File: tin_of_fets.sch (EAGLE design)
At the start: 49 parts, among them Q1 J112, Q2 J112, Q3 ZVN4306A, Q4 ZVN4306A, Q5 J112, Q6 J112, Q7 ZVN4306A, Q8 ZVN4306A, T1 ZTX694B

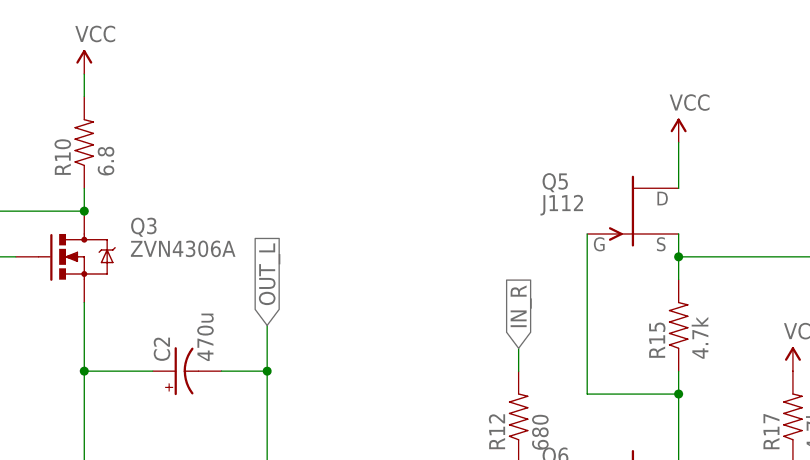
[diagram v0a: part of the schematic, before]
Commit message: Single bypass cap. No more room
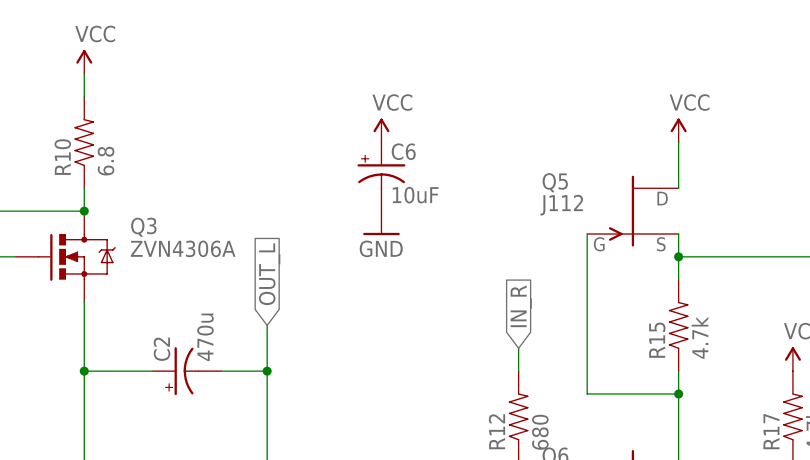
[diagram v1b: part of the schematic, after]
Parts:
- added C6: 10uF, SparkFun-Capacitors:CAP_POLPTH2
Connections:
- net GND: now also C6.-
- net VCC: now also C6.+
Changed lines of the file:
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@@
 <grid distance="0.1" unitdist="inch" unit="inch" style="lines" multiple="1" display="no" altdistance="0.01" altunitdist="inch" altunit="inch"/>
 <layers>
-<layer number="1" name="Top" color="4" fill="1" visible="yes" active="no"/>
-<layer number="16" name="Bottom" color="1" fill="1" visible="yes" active="no"/>
-<layer number="17" name="Pads" color="2" fill="1" visible="yes" active="no"/>
-<layer number="18" name="Vias" color="2" fill="1" visible="yes" active="no"/>
-<layer number="19" name="Unrouted" color="6" fill="1" visible="yes" active="no"/>
-<layer number="20" name="Dimension" color="15" fill="1" visible="yes" active="no"/>
-<layer number="21" name="tPlace" color="7" fill="1" visible="yes" active="no"/>
-<layer number="22" name="bPlace" color="7" fill="1" visible="yes" active="no"/>
-<layer number="23" name="tOrigins" color="15" fill="1" visible="yes" active="no"/>
-<layer number="24" name="bOrigins" color="15" fill="1" visible="yes" active="no"/>
-<layer number="25" name="tNames" color="7" fill="1" visible="yes" active="no"/>
-<layer number="26" name="bNames" color="7" fill="1" visible="yes" active="no"/>
-<layer number="27" name="tValues" color="7" fill="1" visible="yes" active="no"/>
-<layer number="28" name="bValues" color="7" fill="1" visible="yes" active="no"/>
+<layer number="1" name="Top" color="4" fill="1" visible="no" active="no"/>
+<layer number="16" name="Bottom" color="1" fill="1" visible="no" active="no"/>
+<layer number="17" name="Pads" color="2" fill="1" visible="no" active="no"/>
+<layer number="18" name="Vias" color="2" fill="1" visible="no" active="no"/>
+<layer number="19" name="Unrouted" color="6" fill="1" visible="no" active="no"/>
+<layer number="20" name="Dimension" color="15" fill="1" visible="no" active="no"/>
+<layer number="21" name="tPlace" color="7" fill="1" visible="no" active="no"/>
+<layer number="22" name="bPlace" color="7" fill="1" visible="no" active="no"/>
+<layer number="23" name="tOrigins" color="15" fill="1" visible="no" active="no"/>
+<layer number="24" name="bOrigins" color="15" fill="1" visible="no" active="no"/>
+<layer number="25" name="tNames" color="7" fill="1" visible="no" active="no"/>
+<layer number="26" name="bNames" color="7" fill="1" visible="no" active="no"/>
+<layer number="27" name="tValues" color="7" fill="1" visible="no" active="no"/>
+<layer number="28" name="bValues" color="7" fill="1" visible="no" active="no"/>
 <layer number="29" name="tStop" color="7" fill="3" visible="no" active="no"/>
 <layer number="30" name="bStop" color="7" fill="6" visible="no" active="no"/>
@@
 <layer number="35" name="tGlue" color="7" fill="4" visible="no" active="no"/>
 <layer number="36" name="bGlue" color="7" fill="5" visible="no" active="no"/>
-<layer number="37" name="tTest" color="7" fill="1" visible="yes" active="no"/>
-<layer number="38" name="bTest" color="7" fill="1" visible="yes" active="no"/>
+<layer number="37" name="tTest" color="7" fill="1" visible="no" active="no"/>
+<layer number="38" name="bTest" color="7" fill="1" visible="no" active="no"/>
 <layer number="39" name="tKeepout" color="4" fill="11" visible="no" active="no"/>
 <layer number="40" name="bKeepout" color="1" fill="11" visible="no" active="no"/>
@@
 <layer number="44" name="Drills" color="7" fill="1" visible="no" active="no"/>
 <layer number="45" name="Holes" color="7" fill="1" visible="no" active="no"/>
-<layer number="46" name="Milling" color="3" fill="1" visible="yes" active="no"/>
-<layer number="47" name="Measures" color="7" fill="1" visible="yes" active="no"/>
-<layer number="48" name="Document" color="7" fill="1" visible="yes" active="no"/>
-<layer number="49" name="Reference" color="7" fill="1" visible="yes" active="no"/>
-<layer number="50" name="dxf" color="7" fill="1" visible="yes" active="no"/>
-<layer number="51" name="tDocu" color="7" fill="1" visible="yes" active="no"/>
-<layer number="52" name="bDocu" color="7" fill="1" visible="yes" active="no"/>
-<layer number="53" name="tGND_GNDA" color="7" fill="9" visible="yes" active="no"/>
-<layer number="54" name="bGND_GNDA" color="1" fill="9" visible="yes" active="no"/>
-<layer number="56" name="wert" color="7" fill="1" visible="yes" active="no"/>
-<layer number="57" name="tCAD" color="7" fill="1" visible="yes" active="no"/>
-<layer number="59" name="tCarbon" color="7" fill="1" visible="yes" active="no"/>
-<layer number="60" name="bCarbon" color="7" fill="1" visible="yes" active="no"/>
+<layer number="46" name="Milling" color="3" fill="1" visible="no" active="no"/>
+<layer number="47" name="Measures" color="7" fill="1" visible="no" active="no"/>
+<layer number="48" name="Document" color="7" fill="1" visible="no" active="no"/>
+<layer number="49" name="Reference" color="7" fill="1" visible="no" active="no"/>
+<layer number="50" name="dxf" color="7" fill="1" visible="no" active="no"/>
+<layer number="51" name="tDocu" color="7" fill="1" visible="no" active="no"/>
+<layer number="52" name="bDocu" color="7" fill="1" visible="no" active="no"/>
+<layer number="53" name="tGND_GNDA" color="7" fill="9" visible="no" active="no"/>
+<layer number="54" name="bGND_GNDA" color="1" fill="9" visible="no" active="no"/>
+<layer number="56" name="wert" color="7" fill="1" visible="no" active="no"/>
+<layer number="57" name="tCAD" color="7" fill="1" visible="no" active="no"/>
+<layer number="59" name="tCarbon" color="7" fill="1" visible="no" active="no"/>
+<layer number="60" name="bCarbon" color="7" fill="1" visible="no" active="no"/>
 <layer number="90" name="Modules" color="5" fill="1" visible="yes" active="yes"/>
 <layer number="91" name="Nets" color="2" fill="1" visible="yes" active="yes"/>
@@
 <part name="J4" library="SparkFun-Connectors" deviceset="AUDIO-JACK" device="2.5MM"/>
 <part name="GND12" library="SparkFun-Aesthetics" deviceset="GND" device=""/>
+<part name="C6" library="SparkFun-Capacitors" deviceset="CAP_POL" device="PTH2" value="10uF"/>
+<part name="GND11" library="SparkFun-Aesthetics" deviceset="GND" device=""/>
+<part name="SUPPLY8" library="SparkFun-Aesthetics" deviceset="VCC" device=""/>
 </parts>
 <sheets>
@@
 <instance part="J4" gate="G$1" x="91.44" y="78.74"/>
 <instance part="GND12" gate="1" x="101.6" y="81.28" rot="R90"/>
+<instance part="C6" gate="G$1" x="139.7" y="162.56"/>
+<instance part="GND11" gate="1" x="139.7" y="154.94"/>
+<instance part="SUPPLY8" gate="G$1" x="139.7" y="165.1"/>
 </instances>
 <busses>
@@
 <junction x="96.52" y="81.28"/>
 </segment>
+<segment>
+<pinref part="C6" gate="G$1" pin="-"/>
+<pinref part="GND11" gate="1" pin="GND"/>
+</segment>
 </net>
 <net name="N$6" class="0">
@@
 <wire x1="210.82" y1="63.5" x2="218.44" y2="63.5" width="0.1524" layer="91"/>
 </segment>
-</net>
+<segment>
+<pinref part="C6" gate="G$1" pin="+"/>
+<pinref part="SUPPLY8" gate="G$1" pin="VCC"/>
+</segment>
+</net>

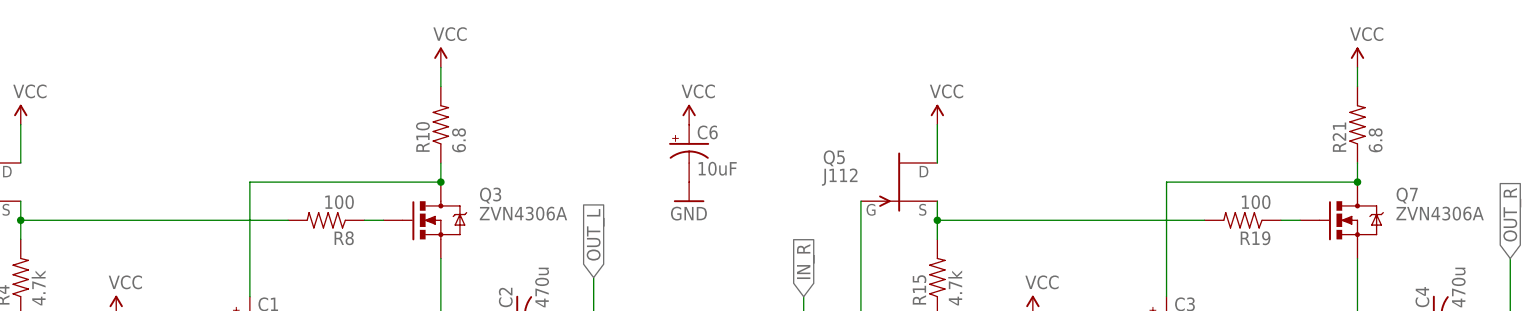
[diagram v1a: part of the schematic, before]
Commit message: Added pads for hand-wiring bypass caps
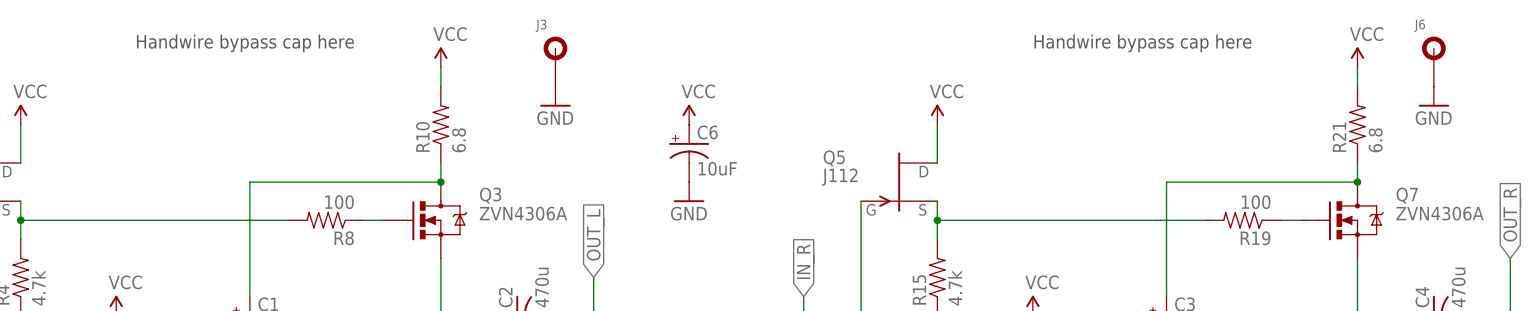
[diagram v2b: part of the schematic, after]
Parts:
- added J3, J6: PAD-NO-THERMAL, my:PAD-NO-THERMAL
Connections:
- net GND: now also J3.P$1, J6.P$1
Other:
- note added: "Handwire bypass cap here"
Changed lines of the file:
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@@
 <part name="GND11" library="SparkFun-Aesthetics" deviceset="GND" device=""/>
 <part name="SUPPLY8" library="SparkFun-Aesthetics" deviceset="VCC" device=""/>
+<part name="J3" library="my" deviceset="PAD-NO-THERMAL" device=""/>
+<part name="GND16" library="SparkFun-Aesthetics" deviceset="GND" device=""/>
+<part name="J6" library="my" deviceset="PAD-NO-THERMAL" device=""/>
+<part name="GND17" library="SparkFun-Aesthetics" deviceset="GND" device=""/>
 </parts>
 <sheets>
 <sheet>
 <plain>
+<text x="66.04" y="175.26" size="1.778" layer="97">Handwire bypass cap here</text>
+<text x="185.42" y="175.26" size="1.778" layer="97">Handwire bypass cap here</text>
 </plain>
 <instances>
@@
 <instance part="GND11" gate="1" x="139.7" y="154.94"/>
 <instance part="SUPPLY8" gate="G$1" x="139.7" y="165.1"/>
+<instance part="J3" gate="G$1" x="121.92" y="175.26"/>
+<instance part="GND16" gate="1" x="121.92" y="167.64"/>
+<instance part="J6" gate="G$1" x="238.76" y="175.26"/>
+<instance part="GND17" gate="1" x="238.76" y="167.64"/>
 </instances>
 <busses>
@@
 <pinref part="GND11" gate="1" pin="GND"/>
 </segment>
-</net>
+<segment>
+<pinref part="J3" gate="G$1" pin="P$1"/>
+<pinref part="GND16" gate="1" pin="GND"/>
+</segment>
+<segment>
+<pinref part="J6" gate="G$1" pin="P$1"/>
+<pinref part="GND17" gate="1" pin="GND"/>
+</segment>
+</net>

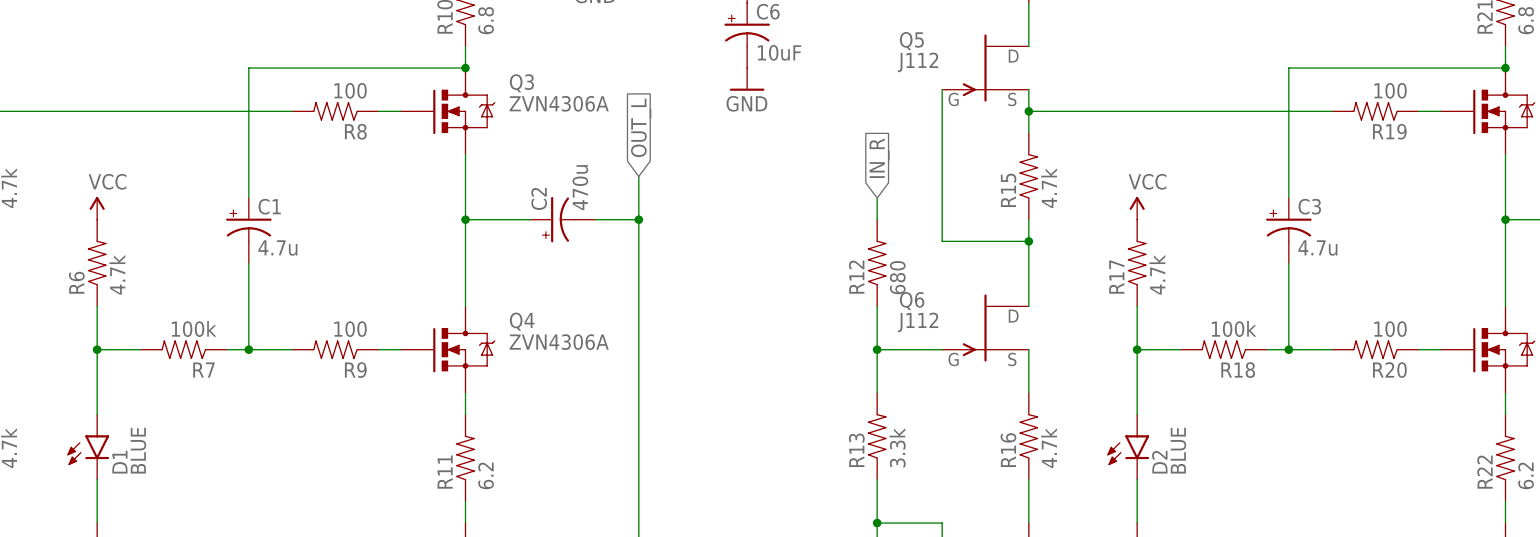
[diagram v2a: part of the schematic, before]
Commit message: Followers FB caps changed to .47u film
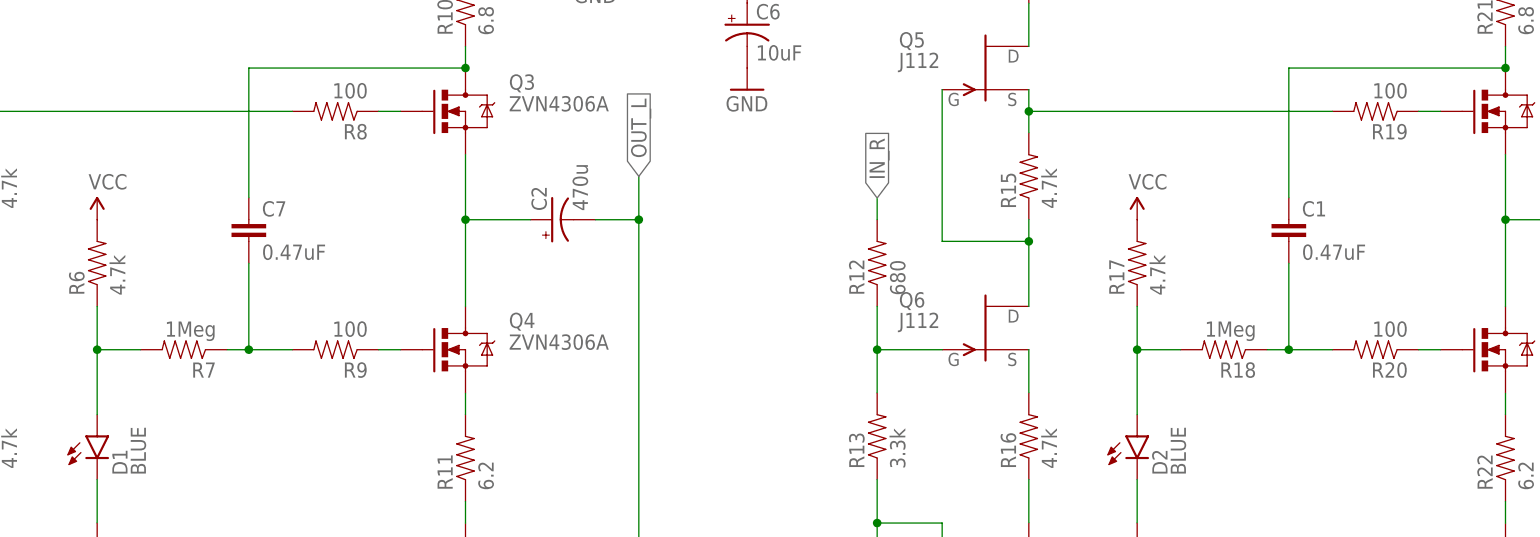
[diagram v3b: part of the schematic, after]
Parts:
- removed C3: 4.7u, SparkFun-Capacitors:CAP_POLPTH2
- added C7: 0.47uF, capacitor-wima:C5/3.5
- C1: value 4.7u -> 0.47uF; device SparkFun-Capacitors:CAP_POLPTH2 -> capacitor-wima:C5/3.5
- R18, R7: value 100k -> 1Meg
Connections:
- net N$11: now also C7.1; no longer C1.+
- net N$13: now also C7.2; no longer C1.-
- net N$20: now also C1.1; no longer C3.+
- net N$21: now also C1.2; no longer C3.-
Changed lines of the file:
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@@
 <part name="GND6" library="SparkFun-Aesthetics" deviceset="GND" device=""/>
 <part name="SUPPLY3" library="SparkFun-Aesthetics" deviceset="VCC" device=""/>
-<part name="C1" library="SparkFun-Capacitors" deviceset="CAP_POL" device="PTH2" value="4.7u"/>
-<part name="R7" library="my-res" deviceset="RESISTOR" device="PTH-1/4W-VERT-SM" value="100k"/>
+<part name="R7" library="my-res" deviceset="RESISTOR" device="PTH-1/4W-VERT-SM" value="1Meg"/>
 <part name="D1" library="SparkFun-LED" deviceset="LED" device="3MM" value="BLUE"/>
 <part name="R6" library="my-res" deviceset="RESISTOR" device="PTH-1/4W-VERT-SM" value="4.7k"/>
@@
 <part name="GND10" library="SparkFun-Aesthetics" deviceset="GND" device=""/>
 <part name="SUPPLY6" library="SparkFun-Aesthetics" deviceset="VCC" device=""/>
-<part name="C3" library="SparkFun-Capacitors" deviceset="CAP_POL" device="PTH2" value="4.7u"/>
-<part name="R18" library="my-res" deviceset="RESISTOR" device="PTH-1/4W-VERT-SM" value="100k"/>
+<part name="R18" library="my-res" deviceset="RESISTOR" device="PTH-1/4W-VERT-SM" value="1Meg"/>
 <part name="D2" library="SparkFun-LED" deviceset="LED" device="3MM" value="BLUE"/>
 <part name="R17" library="my-res" deviceset="RESISTOR" device="PTH-1/4W-VERT-SM" value="4.7k"/>
@@
 <part name="J6" library="my" deviceset="PAD-NO-THERMAL" device=""/>
 <part name="GND17" library="SparkFun-Aesthetics" deviceset="GND" device=""/>
+<part name="C7" library="capacitor-wima" deviceset="C" device="5/3.5" value="0.47uF"/>
+<part name="C1" library="capacitor-wima" deviceset="C" device="5/3.5" value="0.47uF"/>
 </parts>
 <sheets>
@@
 <instance part="GND6" gate="1" x="106.68" y="101.6"/>
 <instance part="SUPPLY3" gate="G$1" x="106.68" y="172.72"/>
-<instance part="C1" gate="G$1" x="81.28" y="139.7"/>
 <instance part="R7" gate="G$1" x="73.66" y="124.46" rot="R180"/>
 <instance part="D1" gate="G$1" x="63.5" y="114.3"/>
@@
 <instance part="GND10" gate="1" x="228.6" y="101.6"/>
 <instance part="SUPPLY6" gate="G$1" x="228.6" y="172.72"/>
-<instance part="C3" gate="G$1" x="203.2" y="139.7"/>
 <instance part="R18" gate="G$1" x="195.58" y="124.46" rot="R180"/>
 <instance part="D2" gate="G$1" x="185.42" y="114.3"/>
@@
 <instance part="J6" gate="G$1" x="238.76" y="175.26"/>
 <instance part="GND17" gate="1" x="238.76" y="167.64"/>
+<instance part="C7" gate="G$1" x="81.28" y="139.7"/>
+<instance part="C1" gate="G$1" x="203.2" y="139.7"/>
 </instances>
 <busses>
@@
 <pinref part="R10" gate="G$1" pin="1"/>
 <wire x1="106.68" y1="157.48" x2="106.68" y2="160.02" width="0.1524" layer="91"/>
-<pinref part="C1" gate="G$1" pin="+"/>
 <wire x1="81.28" y1="142.24" x2="81.28" y2="157.48" width="0.1524" layer="91"/>
 <wire x1="81.28" y1="157.48" x2="106.68" y2="157.48" width="0.1524" layer="91"/>
 <junction x="106.68" y="157.48"/>
+<pinref part="C7" gate="G$1" pin="1"/>
 </segment>
 </net>
@@
 <pinref part="R9" gate="G$1" pin="2"/>
 <wire x1="78.74" y1="124.46" x2="81.28" y2="124.46" width="0.1524" layer="91"/>
-<pinref part="C1" gate="G$1" pin="-"/>
 <wire x1="81.28" y1="124.46" x2="86.36" y2="124.46" width="0.1524" layer="91"/>
 <wire x1="81.28" y1="134.62" x2="81.28" y2="124.46" width="0.1524" layer="91"/>
 <junction x="81.28" y="124.46"/>
+<pinref part="C7" gate="G$1" pin="2"/>
 </segment>
 </net>
@@
 <pinref part="R21" gate="G$1" pin="1"/>
 <wire x1="228.6" y1="157.48" x2="228.6" y2="160.02" width="0.1524" layer="91"/>
-<pinref part="C3" gate="G$1" pin="+"/>
 <wire x1="203.2" y1="142.24" x2="203.2" y2="157.48" width="0.1524" layer="91"/>
 <wire x1="203.2" y1="157.48" x2="228.6" y2="157.48" width="0.1524" layer="91"/>
 <junction x="228.6" y="157.48"/>
+<pinref part="C1" gate="G$1" pin="1"/>
 </segment>
 </net>
@@
 <pinref part="R20" gate="G$1" pin="2"/>
 <wire x1="200.66" y1="124.46" x2="203.2" y2="124.46" width="0.1524" layer="91"/>
-<pinref part="C3" gate="G$1" pin="-"/>
 <wire x1="203.2" y1="124.46" x2="208.28" y2="124.46" width="0.1524" layer="91"/>
 <wire x1="203.2" y1="134.62" x2="203.2" y2="124.46" width="0.1524" layer="91"/>
 <junction x="203.2" y="124.46"/>
-</segment>
-</net>
+<pinref part="C1" gate="G$1" pin="2"/>
+</segment>
+</net>

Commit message: Jacks pinout fixed
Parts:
- J1, J2, J4: device SparkFun-Connectors:AUDIO-JACK2.5MM -> my-conn:AUDIO-JACK2.5MM
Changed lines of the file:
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@@
 <part name="GND9" library="SparkFun-Aesthetics" deviceset="GND" device=""/>
 <part name="SUPPLY5" library="SparkFun-Aesthetics" deviceset="VCC" device=""/>
-<part name="J1" library="SparkFun-Connectors" deviceset="AUDIO-JACK" device="2.5MM"/>
-<part name="J2" library="SparkFun-Connectors" deviceset="AUDIO-JACK" device="2.5MM"/>
+<part name="J1" library="my-conn" deviceset="AUDIO-JACK" device="2.5MM"/>
+<part name="J2" library="my-conn" deviceset="AUDIO-JACK" device="2.5MM"/>
 <part name="GND2" library="SparkFun-Aesthetics" deviceset="GND" device=""/>
 <part name="GND3" library="SparkFun-Aesthetics" deviceset="GND" device=""/>
@@
 <part name="SUPPLY7" library="SparkFun-Aesthetics" deviceset="VCC" device=""/>
 <part name="J5" library="SparkFun-Connectors" deviceset="M01" device="PTH"/>
-<part name="J4" library="SparkFun-Connectors" deviceset="AUDIO-JACK" device="2.5MM"/>
+<part name="J4" library="my-conn" deviceset="AUDIO-JACK" device="2.5MM"/>
 <part name="GND12" library="SparkFun-Aesthetics" deviceset="GND" device=""/>
 <part name="C6" library="SparkFun-Capacitors" deviceset="CAP_POL" device="PTH2" value="10uF"/>
